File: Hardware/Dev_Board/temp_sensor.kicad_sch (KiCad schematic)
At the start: 2 parts

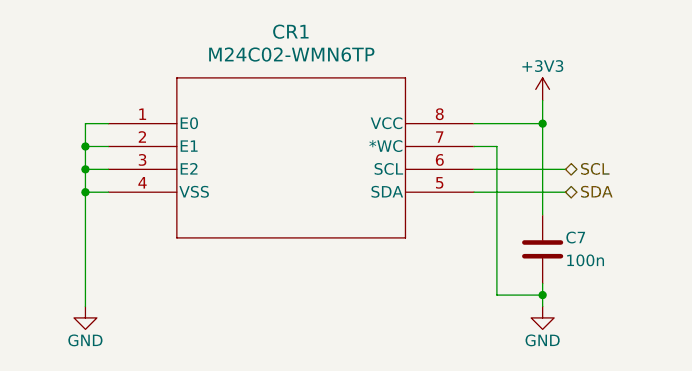
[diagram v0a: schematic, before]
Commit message: Added the temperature sensor
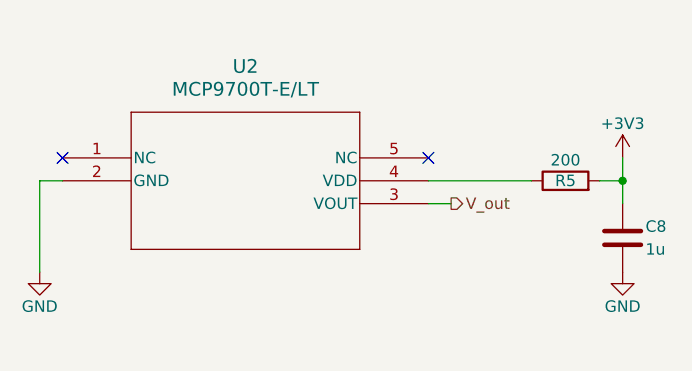
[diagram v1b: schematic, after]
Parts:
- removed C7: 100n, symbol Device:C
- removed CR1: M24C02-WMN6TP, SO-8_STM, symbol Dev_Board:M24C02-WMN6TP
- added C8: 1u, symbol Device:C
- added R5: 200, symbol Device:R
- added U2: MCP9700T-E/LT, SC70-5_MC_MCH, symbol Dev_Board:MCP9700T-E_LT
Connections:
- net +3V3: now also C8.1, R5.2
- net GND: now also C8.2, U2.2 (GND)
- new net: R5.1, U2.4 (VDD)
- new net V_out: U2.3 (VOUT)
- no-connect marks 0 -> 2
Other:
- title: EEPROM -> Temperature Sensor
